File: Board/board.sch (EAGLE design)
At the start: 4 parts, among them IC1 L293D

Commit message: various stuff and board
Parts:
- removed R1, R2: (no value), adafruit:R-US_0204/5
- added ALIM, BUZZ, MOT1, MOT2: (no value), pinhead:PINHD-1X2
- added PHOTO: (no value), pinhead:PINHD-2X3
- added R3: 10k, BaseApp:RESISTOR
- added S1, S3, SW1, SW2, SW3: (no value), adafruit:40-XX
- added SRVO, ULTRA: (no value), pinhead:PINHD-1X3
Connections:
- new net N$1: IC1.1Y, MOT1.2
- new net N$10: IC1.1-2EN, PCB1.~11
- new net N$11: PCB1.A1, PHOTO.6
- new net N$12: PCB1.A0, PHOTO.4
- new net N$13: PHOTO.2
- new net N$14: PCB1.~6, SRVO.2
- new net N$15: PCB1.~3, ULTRA.2
- new net N$16: BUZZ.1, PCB1.~5
- new net N$17: PCB1.7, SW3.P
- new net N$18: R3.2, SW3.P1
- new net N$19: PCB1.4, SW2.P
- new net N$2: IC1.2Y, MOT1.1
- new net N$3: IC1.3Y, MOT2.2
- new net N$4: IC1.4Y, MOT2.1
- new net N$5: IC1.1A, PCB1.12
- new net N$6: IC1.2A, PCB1.13
- new net N$7: IC1.4A, PCB1.~10
- new net N$8: IC1.3-4EN, PCB1.~9
- new net N$9: IC1.3A, PCB1.8
- net +5V: now also ALIM.2, IC1.VCC1, IC1.VCC2, PHOTO.1, PHOTO.3, PHOTO.5, SRVO.1, SW1.S, SW2.S1, SW3.S, ULTRA.1
- net GND: now also ALIM.1, BUZZ.2, IC1.GND1, IC1.GND2, IC1.GND3, IC1.GND4, PCB1.28(SCL), R3.1, SRVO.3, ULTRA.3; no longer PCB1.GND
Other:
- moved on the sheet: IC1

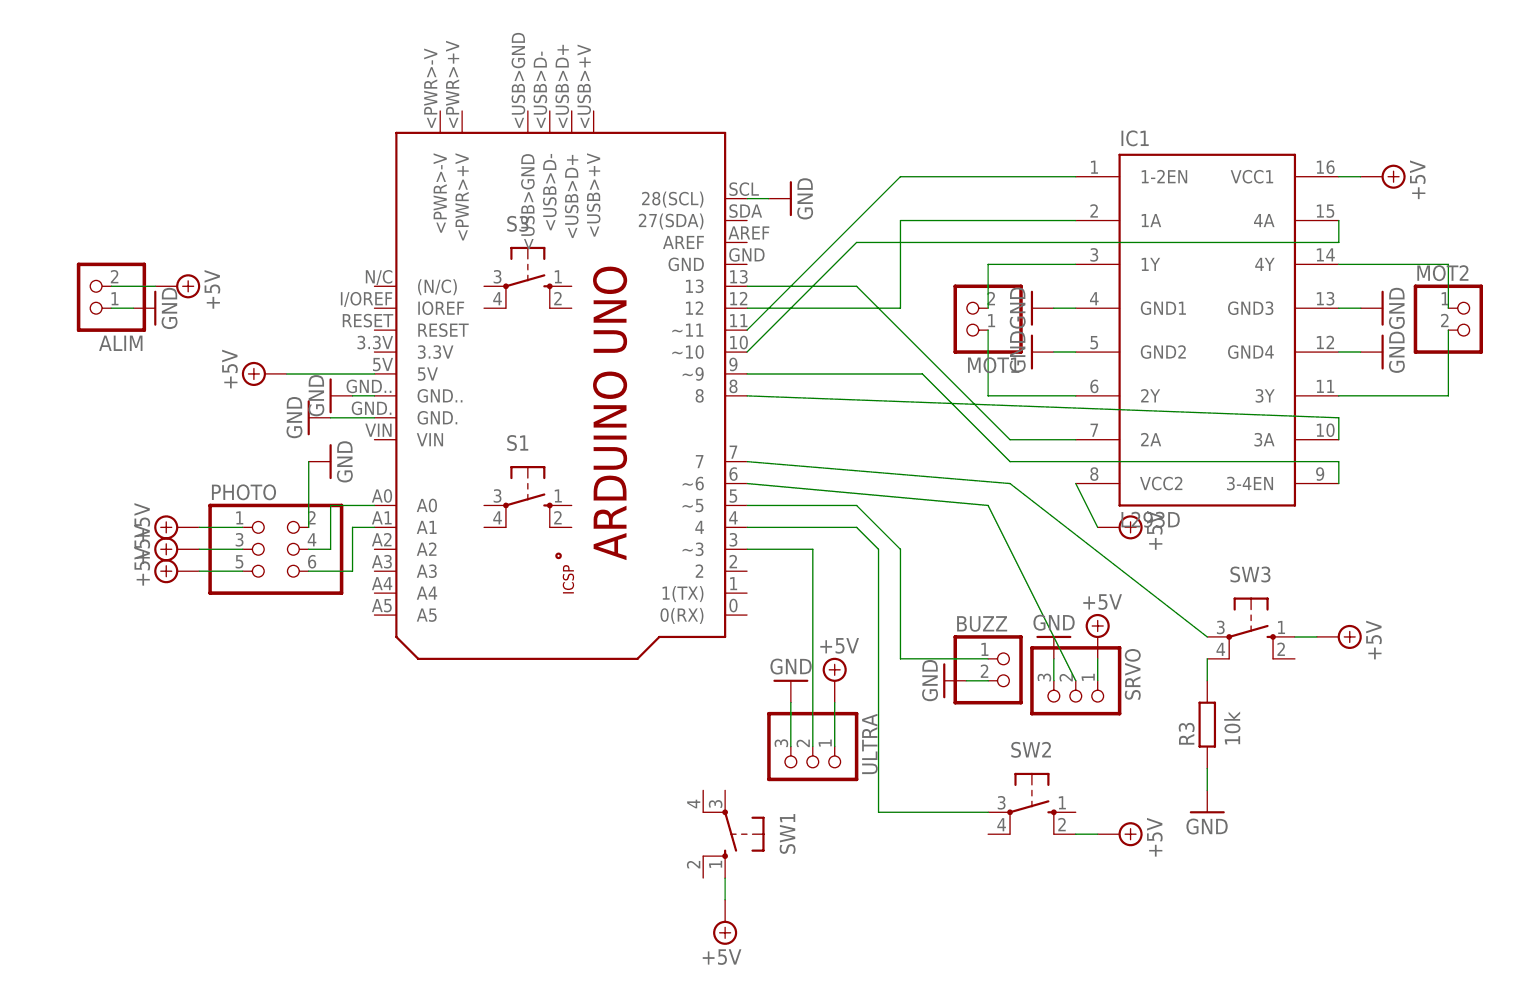
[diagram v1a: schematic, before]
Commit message: Eagle : Switches connected, useless backups deleted
- Connected the switches left unconnected last time
- Optimized the schematics
- Removed the now useless backups & libraries - only kept the 3 most
recent versions.
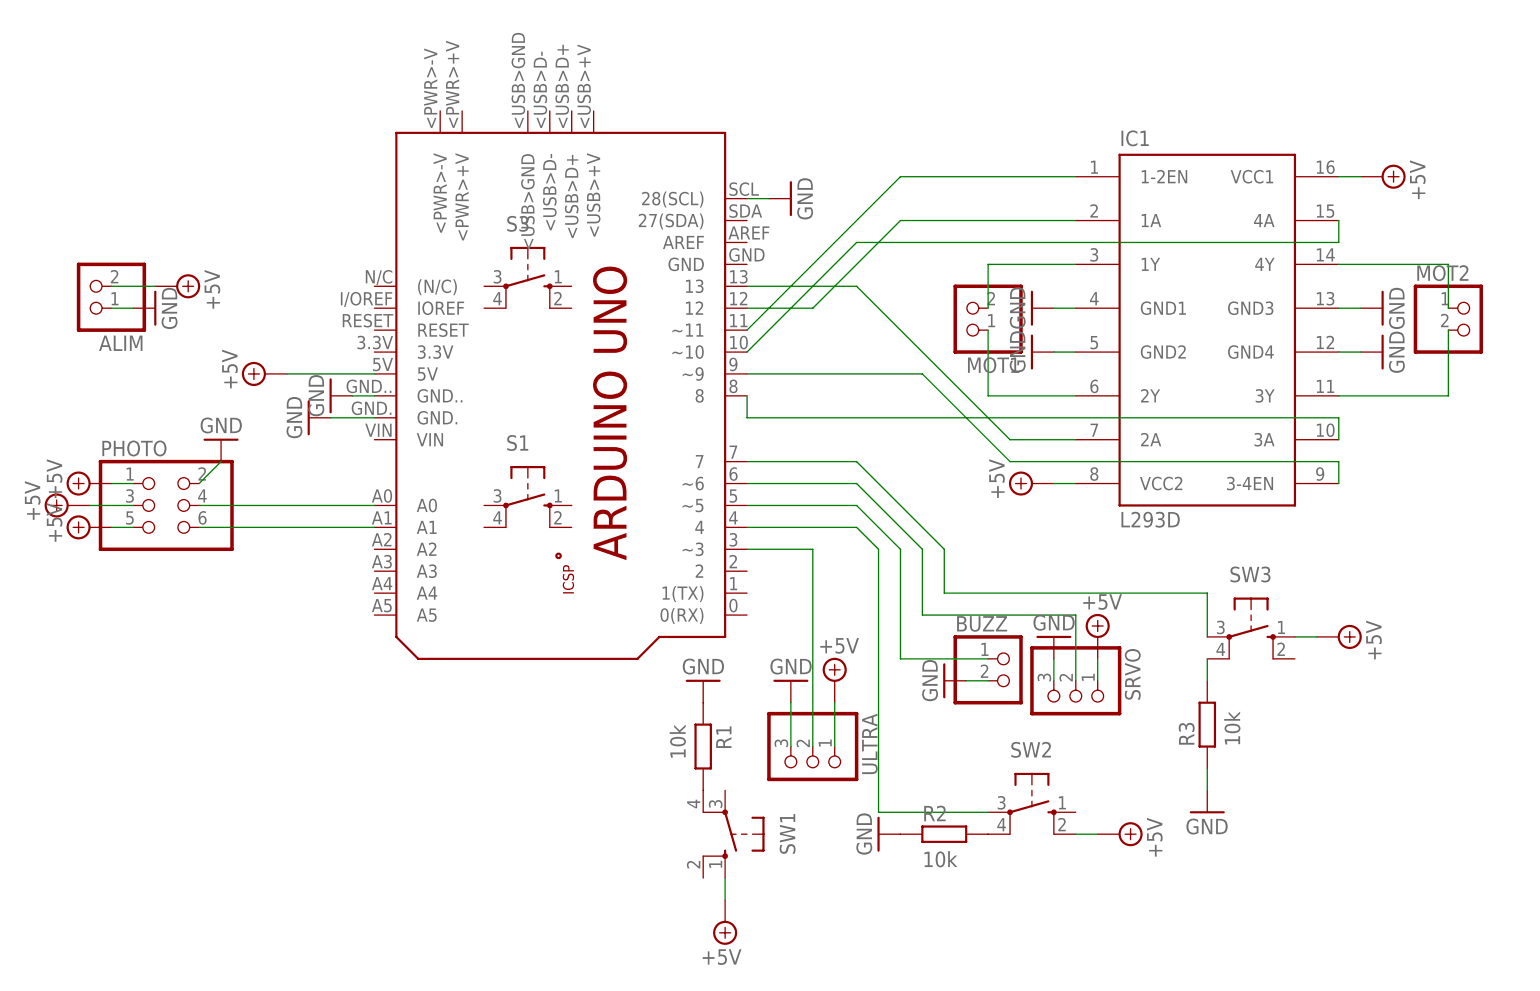
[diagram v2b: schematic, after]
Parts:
- added R1, R2: 10k, BaseApp:RESISTOR
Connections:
- new net N$20: R2.2, SW2.P1
- new net N$21: R1.2, SW1.P1
- net GND: now also R1.1, R2.1
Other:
- moved on the sheet: PHOTO
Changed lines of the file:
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@@
 <part name="SUPPLY12" library="supply2" deviceset="+5V" device=""/>
 <part name="GND12" library="supply1" deviceset="GND" device=""/>
+<part name="R2" library="BaseApp" deviceset="RESISTOR" device="" value="10k"/>
+<part name="R1" library="BaseApp" deviceset="RESISTOR" device="" value="10k"/>
+<part name="GND14" library="supply1" deviceset="GND" device=""/>
+<part name="GND15" library="supply1" deviceset="GND" device=""/>
 </parts>
 <sheets>
@@
 <instance part="SUPPLY1" gate="+5V" x="27.94" y="53.34" rot="R90"/>
 <instance part="SUPPLY2" gate="+5V" x="157.48" y="76.2" rot="R270"/>
-<instance part="SUPPLY3" gate="+5V" x="127" y="35.56" rot="R270"/>
+<instance part="SUPPLY3" gate="+5V" x="116.84" y="40.64" rot="R90"/>
 <instance part="GND3" gate="1" x="33.02" y="48.26" rot="R270"/>
 <instance part="GND4" gate="1" x="35.56" y="50.8" rot="R270"/>
@@
 <instance part="GND10" gate="1" x="88.9" y="17.78" rot="R180"/>
 <instance part="BUZZ" gate="G$1" x="114.3" y="17.78"/>
-<instance part="PHOTO" gate="A" x="27.94" y="33.02"/>
-<instance part="SUPPLY7" gate="+5V" x="17.78" y="35.56" rot="R90"/>
-<instance part="SUPPLY8" gate="+5V" x="17.78" y="33.02" rot="R90"/>
-<instance part="SUPPLY9" gate="+5V" x="17.78" y="30.48" rot="R90"/>
-<instance part="GND11" gate="1" x="35.56" y="43.18" rot="R90"/>
+<instance part="PHOTO" gate="A" x="15.24" y="38.1"/>
+<instance part="SUPPLY7" gate="+5V" x="7.62" y="40.64" rot="R90"/>
+<instance part="SUPPLY8" gate="+5V" x="5.08" y="38.1" rot="R90"/>
+<instance part="SUPPLY9" gate="+5V" x="7.62" y="35.56" rot="R90"/>
+<instance part="GND11" gate="1" x="22.86" y="45.72" rot="R180"/>
 <instance part="S1" gate="1" x="58.42" y="38.1" rot="R270"/>
 <instance part="SW3" gate="1" x="142.24" y="22.86" rot="R270"/>
@@
 <instance part="SUPPLY12" gate="+5V" x="81.28" y="-10.16" rot="R180"/>
 <instance part="GND12" gate="1" x="106.68" y="17.78" rot="R270"/>
+<instance part="R2" gate="G$1" x="106.68" y="0"/>
+<instance part="R1" gate="G$1" x="78.74" y="10.16" rot="R270"/>
+<instance part="GND14" gate="1" x="78.74" y="17.78" rot="R180"/>
+<instance part="GND15" gate="1" x="99.06" y="0" rot="R270"/>
 </instances>
 <busses>
@@
 <pinref part="GND12" gate="1" pin="GND"/>
 </segment>
+<segment>
+<pinref part="R2" gate="G$1" pin="1"/>
+<pinref part="GND15" gate="1" pin="GND"/>
+</segment>
+<segment>
+<pinref part="R1" gate="G$1" pin="1"/>
+<pinref part="GND14" gate="1" pin="GND"/>
+</segment>
 </net>
 <net name="+5V" class="0">
@@
 <pinref part="IC1" gate="G$1" pin="VCC2"/>
 <pinref part="SUPPLY3" gate="+5V" pin="+5V"/>
-<wire x1="124.46" y1="35.56" x2="121.92" y2="40.64" width="0.1524" layer="91"/>
+<wire x1="119.38" y1="40.64" x2="121.92" y2="40.64" width="0.1524" layer="91"/>
 </segment>
 <segment>
@@
 <pinref part="PHOTO" gate="A" pin="1"/>
 <pinref part="SUPPLY7" gate="+5V" pin="+5V"/>
-<wire x1="20.32" y1="35.56" x2="25.4" y2="35.56" width="0.1524" layer="91"/>
+<wire x1="10.16" y1="40.64" x2="12.7" y2="40.64" width="0.1524" layer="91"/>
 </segment>
 <segment>
 <pinref part="PHOTO" gate="A" pin="3"/>
 <pinref part="SUPPLY8" gate="+5V" pin="+5V"/>
-<wire x1="20.32" y1="33.02" x2="25.4" y2="33.02" width="0.1524" layer="91"/>
+<wire x1="7.62" y1="38.1" x2="12.7" y2="38.1" width="0.1524" layer="91"/>
 </segment>
 <segment>
 <pinref part="PHOTO" gate="A" pin="5"/>
 <pinref part="SUPPLY9" gate="+5V" pin="+5V"/>
-<wire x1="20.32" y1="30.48" x2="25.4" y2="30.48" width="0.1524" layer="91"/>
+<wire x1="10.16" y1="35.56" x2="12.7" y2="35.56" width="0.1524" layer="91"/>
 </segment>
 <segment>
@@
 <segment>
 <pinref part="PCB1" gate="G$1" pin="12"/>
-<wire x1="83.82" y1="60.96" x2="101.6" y2="60.96" width="0.1524" layer="91"/>
-<wire x1="101.6" y1="60.96" x2="101.6" y2="71.12" width="0.1524" layer="91"/>
+<wire x1="83.82" y1="60.96" x2="91.44" y2="60.96" width="0.1524" layer="91"/>
+<wire x1="91.44" y1="60.96" x2="101.6" y2="71.12" width="0.1524" layer="91"/>
 <pinref part="IC1" gate="G$1" pin="1A"/>
 <wire x1="101.6" y1="71.12" x2="121.92" y2="71.12" width="0.1524" layer="91"/>
@@
 <segment>
 <pinref part="PCB1" gate="G$1" pin="8"/>
-<wire x1="83.82" y1="50.8" x2="152.4" y2="48.26" width="0.1524" layer="91"/>
 <pinref part="IC1" gate="G$1" pin="3A"/>
 <wire x1="152.4" y1="48.26" x2="152.4" y2="45.72" width="0.1524" layer="91"/>
+<wire x1="83.82" y1="50.8" x2="83.82" y2="48.26" width="0.1524" layer="91"/>
+<wire x1="83.82" y1="48.26" x2="152.4" y2="48.26" width="0.1524" layer="91"/>
 </segment>
 </net>
@@
 <segment>
 <pinref part="PHOTO" gate="A" pin="6"/>
-<wire x1="33.02" y1="30.48" x2="38.1" y2="30.48" width="0.1524" layer="91"/>
-<wire x1="38.1" y1="30.48" x2="38.1" y2="35.56" width="0.1524" layer="91"/>
+<wire x1="20.32" y1="35.56" x2="40.64" y2="35.56" width="0.1524" layer="91"/>
 <pinref part="PCB1" gate="G$1" pin="A1"/>
-<wire x1="38.1" y1="35.56" x2="40.64" y2="35.56" width="0.1524" layer="91"/>
 </segment>
 </net>
@@
 <segment>
 <pinref part="PHOTO" gate="A" pin="4"/>
-<wire x1="33.02" y1="33.02" x2="35.56" y2="33.02" width="0.1524" layer="91"/>
-<wire x1="35.56" y1="33.02" x2="35.56" y2="38.1" width="0.1524" layer="91"/>
+<wire x1="20.32" y1="38.1" x2="40.64" y2="38.1" width="0.1524" layer="91"/>
 <pinref part="PCB1" gate="G$1" pin="A0"/>
-<wire x1="35.56" y1="38.1" x2="40.64" y2="38.1" width="0.1524" layer="91"/>
 </segment>
 </net>
@@
 <segment>
 <pinref part="PHOTO" gate="A" pin="2"/>
-<wire x1="33.02" y1="35.56" x2="33.02" y2="43.18" width="0.1524" layer="91"/>
+<wire x1="20.32" y1="40.64" x2="22.86" y2="43.18" width="0.1524" layer="91"/>
 <pinref part="GND11" gate="1" pin="GND"/>
 </segment>
@@
 <pinref part="SRVO" gate="A" pin="2"/>
 <pinref part="PCB1" gate="G$1" pin="~6"/>
-<wire x1="83.82" y1="40.64" x2="111.76" y2="38.1" width="0.1524" layer="91"/>
-<wire x1="111.76" y1="38.1" x2="121.92" y2="17.78" width="0.1524" layer="91"/>
+<wire x1="83.82" y1="40.64" x2="96.52" y2="40.64" width="0.1524" layer="91"/>
+<wire x1="96.52" y1="40.64" x2="104.14" y2="33.02" width="0.1524" layer="91"/>
+<wire x1="104.14" y1="33.02" x2="104.14" y2="25.4" width="0.1524" layer="91"/>
+<wire x1="104.14" y1="25.4" x2="121.92" y2="25.4" width="0.1524" layer="91"/>
+<wire x1="121.92" y1="25.4" x2="121.92" y2="17.78" width="0.1524" layer="91"/>
 </segment>
 </net>
@@
 <segment>
 <pinref part="PCB1" gate="G$1" pin="7"/>
+<wire x1="83.82" y1="43.18" x2="96.52" y2="43.18" width="0.1524" layer="91"/>
+<wire x1="96.52" y1="43.18" x2="106.68" y2="33.02" width="0.1524" layer="91"/>
+<wire x1="106.68" y1="33.02" x2="106.68" y2="27.94" width="0.1524" layer="91"/>
+<wire x1="106.68" y1="27.94" x2="137.16" y2="27.94" width="0.1524" layer="91"/>
 <pinref part="SW3" gate="1" pin="P"/>
-<wire x1="83.82" y1="43.18" x2="114.3" y2="40.64" width="0.1524" layer="91"/>
-<wire x1="114.3" y1="40.64" x2="137.16" y2="22.86" width="0.1524" layer="91"/>
+<wire x1="137.16" y1="27.94" x2="137.16" y2="22.86" width="0.1524" layer="91"/>
 </segment>
 </net>
@@
 </segment>
 </net>
+<net name="N$20" class="0">
+<segment>
+<pinref part="SW2" gate="1" pin="P1"/>
+<pinref part="R2" gate="G$1" pin="2"/>
+</segment>
+</net>
+<net name="N$21" class="0">
+<segment>
+<pinref part="SW1" gate="1" pin="P1"/>
+<pinref part="R1" gate="G$1" pin="2"/>
+</segment>
+</net>

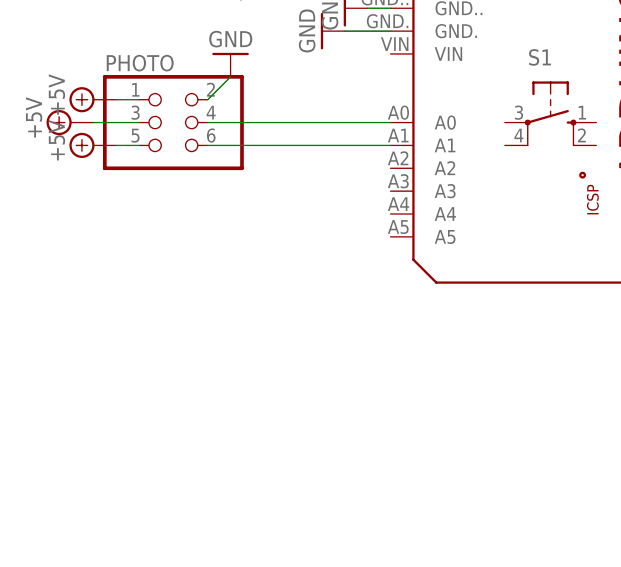
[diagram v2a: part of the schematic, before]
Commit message: Eagle : Added thumbwheels
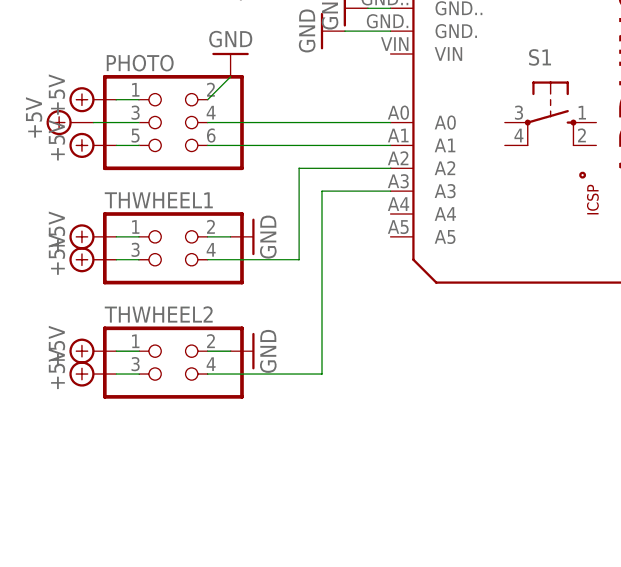
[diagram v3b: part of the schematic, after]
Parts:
- added THWHEEL1, THWHEEL2: (no value), pinhead:PINHD-2X2
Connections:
- new net N$22: PCB1.A2, THWHEEL1.4
- new net N$23: PCB1.A3, THWHEEL2.4
- net +5V: now also THWHEEL1.1, THWHEEL1.3, THWHEEL2.1, THWHEEL2.3
- net GND: now also THWHEEL1.2, THWHEEL2.2
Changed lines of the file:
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@@
 <part name="GND14" library="supply1" deviceset="GND" device=""/>
 <part name="GND15" library="supply1" deviceset="GND" device=""/>
+<part name="THWHEEL1" library="pinhead" deviceset="PINHD-2X2" device=""/>
+<part name="THWHEEL2" library="pinhead" deviceset="PINHD-2X2" device=""/>
+<part name="GND16" library="supply1" deviceset="GND" device=""/>
+<part name="GND17" library="supply1" deviceset="GND" device=""/>
+<part name="SUPPLY13" library="supply2" deviceset="+5V" device=""/>
+<part name="SUPPLY14" library="supply2" deviceset="+5V" device=""/>
+<part name="SUPPLY15" library="supply2" deviceset="+5V" device=""/>
+<part name="SUPPLY16" library="supply2" deviceset="+5V" device=""/>
 </parts>
 <sheets>
@@
 <instance part="GND14" gate="1" x="78.74" y="17.78" rot="R180"/>
 <instance part="GND15" gate="1" x="99.06" y="0" rot="R270"/>
+<instance part="THWHEEL1" gate="A" x="17.78" y="22.86"/>
+<instance part="THWHEEL2" gate="A" x="17.78" y="10.16"/>
+<instance part="GND16" gate="1" x="25.4" y="12.7" rot="R90"/>
+<instance part="GND17" gate="1" x="25.4" y="25.4" rot="R90"/>
+<instance part="SUPPLY13" gate="+5V" x="7.62" y="25.4" rot="R90"/>
+<instance part="SUPPLY14" gate="+5V" x="7.62" y="22.86" rot="R90"/>
+<instance part="SUPPLY15" gate="+5V" x="7.62" y="12.7" rot="R90"/>
+<instance part="SUPPLY16" gate="+5V" x="7.62" y="10.16" rot="R90"/>
 </instances>
 <busses>
@@
 <pinref part="GND14" gate="1" pin="GND"/>
 </segment>
+<segment>
+<pinref part="THWHEEL2" gate="A" pin="2"/>
+<pinref part="GND16" gate="1" pin="GND"/>
+<wire x1="22.86" y1="12.7" x2="20.32" y2="12.7" width="0.1524" layer="91"/>
+</segment>
+<segment>
+<pinref part="THWHEEL1" gate="A" pin="2"/>
+<pinref part="GND17" gate="1" pin="GND"/>
+<wire x1="22.86" y1="25.4" x2="20.32" y2="25.4" width="0.1524" layer="91"/>
+</segment>
 </net>
 <net name="+5V" class="0">
@@
 <pinref part="SUPPLY11" gate="+5V" pin="+5V"/>
 <wire x1="121.92" y1="0" x2="124.46" y2="0" width="0.1524" layer="91"/>
+</segment>
+<segment>
+<pinref part="THWHEEL1" gate="A" pin="1"/>
+<pinref part="SUPPLY13" gate="+5V" pin="+5V"/>
+<wire x1="10.16" y1="25.4" x2="12.7" y2="25.4" width="0.1524" layer="91"/>
+</segment>
+<segment>
+<pinref part="THWHEEL1" gate="A" pin="3"/>
+<pinref part="SUPPLY14" gate="+5V" pin="+5V"/>
+<wire x1="10.16" y1="22.86" x2="12.7" y2="22.86" width="0.1524" layer="91"/>
+</segment>
+<segment>
+<pinref part="THWHEEL2" gate="A" pin="1"/>
+<pinref part="SUPPLY15" gate="+5V" pin="+5V"/>
+<wire x1="10.16" y1="12.7" x2="12.7" y2="12.7" width="0.1524" layer="91"/>
+</segment>
+<segment>
+<pinref part="THWHEEL2" gate="A" pin="3"/>
+<pinref part="SUPPLY16" gate="+5V" pin="+5V"/>
+<wire x1="10.16" y1="10.16" x2="12.7" y2="10.16" width="0.1524" layer="91"/>
 </segment>
 </net>
@@
 </segment>
 </net>
+<net name="N$22" class="0">
+<segment>
+<pinref part="THWHEEL1" gate="A" pin="4"/>
+<wire x1="20.32" y1="22.86" x2="30.48" y2="22.86" width="0.1524" layer="91"/>
+<wire x1="30.48" y1="22.86" x2="30.48" y2="33.02" width="0.1524" layer="91"/>
+<pinref part="PCB1" gate="G$1" pin="A2"/>
+<wire x1="30.48" y1="33.02" x2="40.64" y2="33.02" width="0.1524" layer="91"/>
+</segment>
+</net>
+<net name="N$23" class="0">
+<segment>
+<pinref part="PCB1" gate="G$1" pin="A3"/>
+<wire x1="40.64" y1="30.48" x2="33.02" y2="30.48" width="0.1524" layer="91"/>
+<wire x1="33.02" y1="30.48" x2="33.02" y2="10.16" width="0.1524" layer="91"/>
+<pinref part="THWHEEL2" gate="A" pin="4"/>
+<wire x1="33.02" y1="10.16" x2="20.32" y2="10.16" width="0.1524" layer="91"/>
+</segment>
+</net>
